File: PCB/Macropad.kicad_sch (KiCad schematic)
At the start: 29 parts, among them J1 OLED, SW1 SW_Push, SW11 RotaryEncoder_Switch, SW2 SW_Push, SW3 SW_Push, SW4 SW_Push, SW5 SW_Push, SW6 SW_Push, SW7 SW_Push, SW8 SW_Push, SW9 SW_Push, U1 XIAO-RP2040-DIP

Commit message: Update PCB files
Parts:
- removed D1, D13, D14, D15, D16, D17, D2, D6: SK6812MINI, LED_SMD:LED_SK6812MINI_PLCC4_3.5x3.5mm_P1.75mm, symbol LED:SK6812MINI
- added LED1, LED2, LED3, LED4, LED5, LED6, LED7, LED8: MX_SK6812MINI-E, PCM_marbastlib-choc:LED_choc_6028R, symbol PCM_marbastlib-mx:MX_SK6812MINI-E
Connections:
- net +5V: now also LED1.1 (VDD), LED2.1 (VDD), LED3.1 (VDD), LED4.1 (VDD), LED5.1 (VDD), LED6.1 (VDD), LED7.1 (VDD), LED8.1 (VDD)
- net GND: now also LED1.4 (VSS), LED2.4 (VSS), LED3.4 (VSS), LED4.4 (VSS), LED5.4 (VSS), LED6.4 (VSS), LED7.4 (VSS), LED8.4 (VSS)
- net at U1.8 (GPIO1/RX): now also LED2.3 (DIN)
- new net: LED1.3 (DIN), LED7.2 (DOUT)
- new net: LED6.2 (DOUT), LED7.3 (DIN)
- new net: LED1.2 (DOUT), LED8.3 (DIN)
- new net: LED4.2 (DOUT), LED5.3 (DIN)
- new net: LED3.2 (DOUT), LED4.3 (DIN)
- new net: LED5.2 (DOUT), LED6.3 (DIN)
- new net: LED2.2 (DOUT), LED3.3 (DIN)

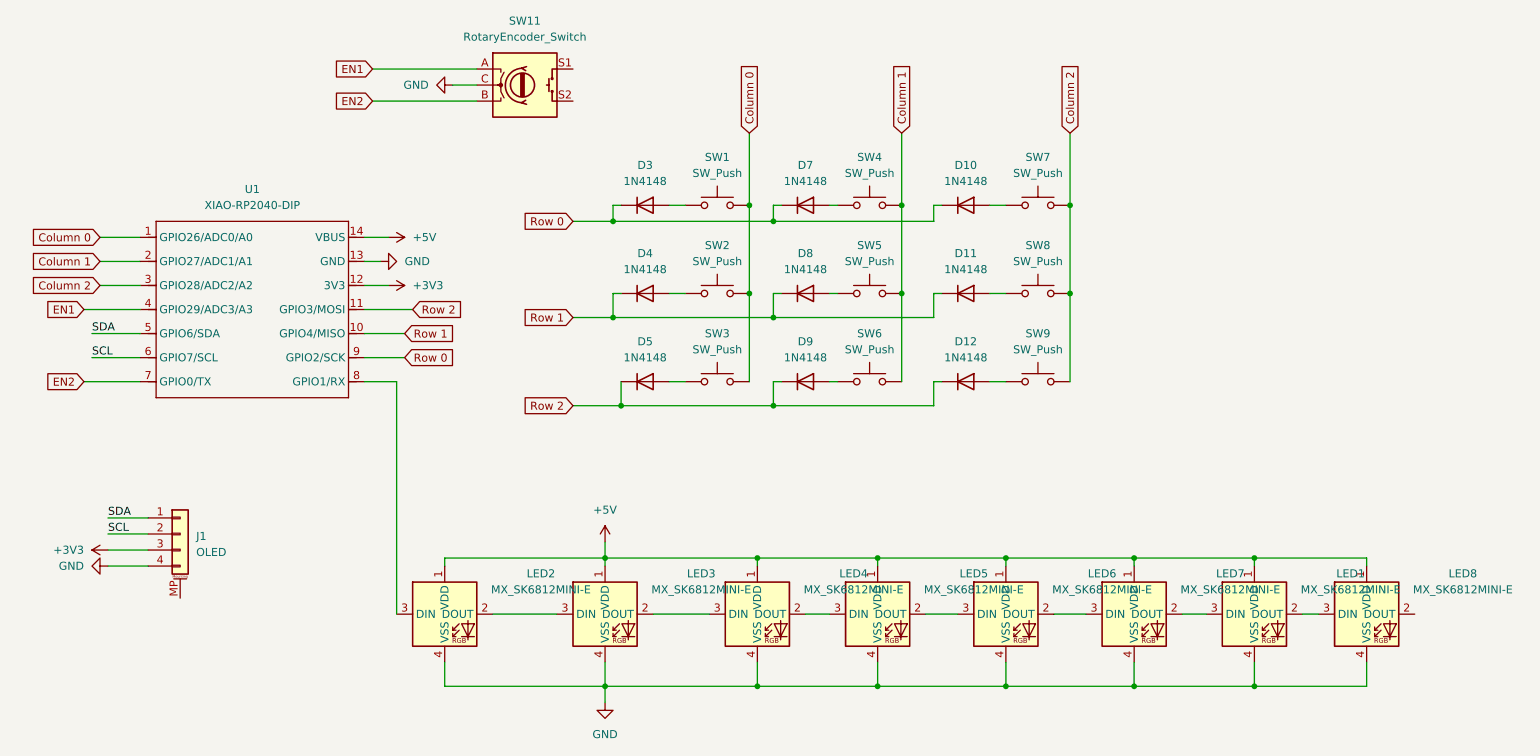
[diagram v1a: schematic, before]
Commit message: Fixed some bugs in the PCB and exported Gerber files.
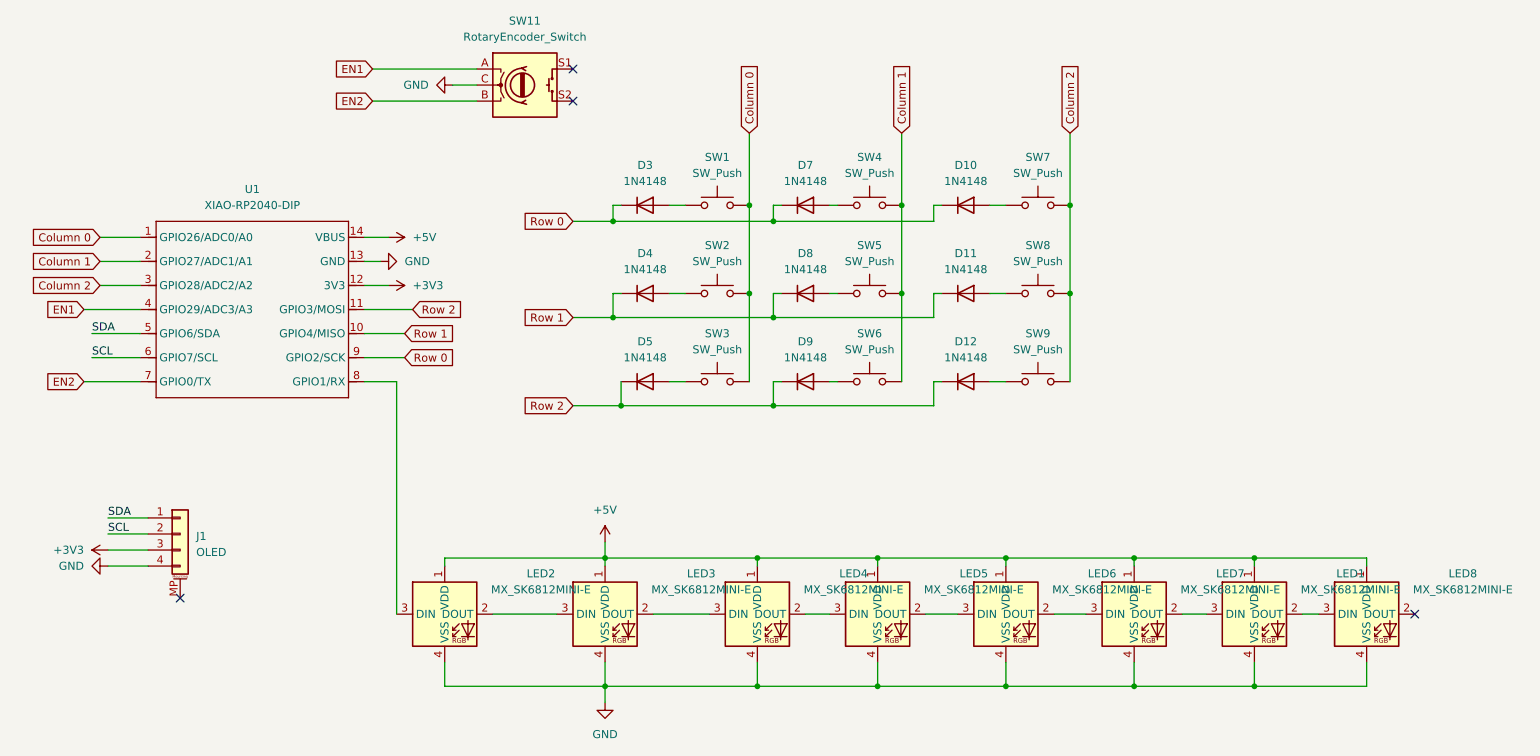
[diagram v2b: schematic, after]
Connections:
- no-connect marks 0 -> 4
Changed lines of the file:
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@@
 		(color 0 0 0 0)
+	)
+	(no_connect
+		(at 120.65 41.91)
+	)
+	(no_connect
+		(at 120.65 36.83)
+	)
+	(no_connect
+		(at 58.42 120.65)
+	)
+	(no_connect
+		(at 254 123.19)
 	)
 	(wire

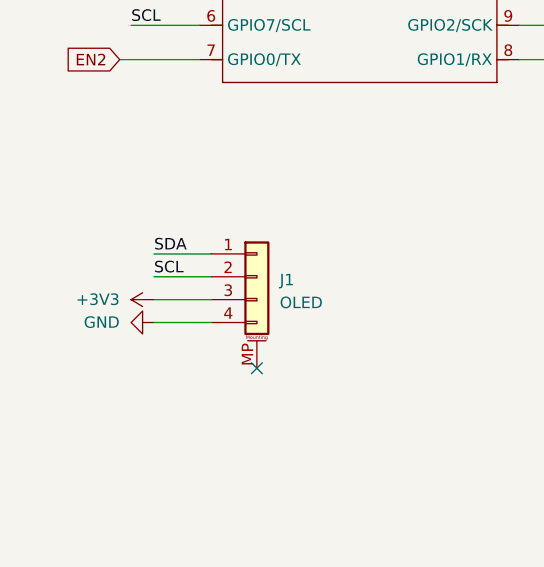
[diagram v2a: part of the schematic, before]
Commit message: Fixed some bugs in the PCB and exported Gerber files again. CAD files have been updated with the latest modifications.
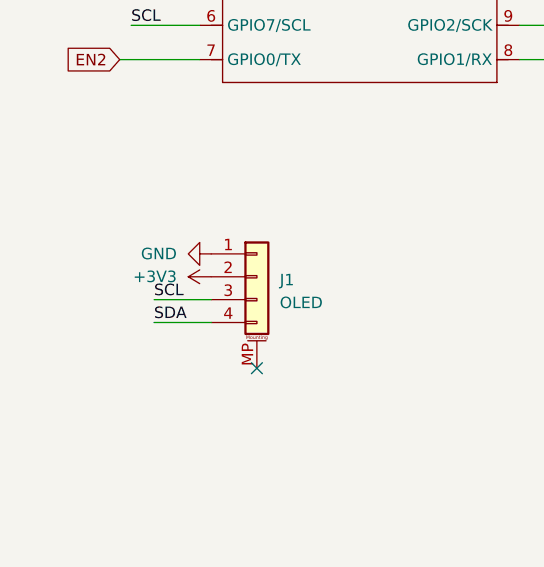
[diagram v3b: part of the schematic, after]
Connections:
- net +3V3: now also J1.2 (Pin_2); no longer J1.3 (Pin_3)
- net GND: now also J1.1 (Pin_1); no longer J1.4 (Pin_4)
- net SCL: now also J1.3 (Pin_3); no longer J1.2 (Pin_2)
- net SDA: now also J1.4 (Pin_4); no longer J1.1 (Pin_1)
